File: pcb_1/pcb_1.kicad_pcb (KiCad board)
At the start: 2 copper layers, 80 parts, among them J1 Screw_Terminal_01x02, J2 Screw_Terminal_01x03, J3 Conn_01x02_Male, J4 Screw_Terminal_01x02, J5 Isolated_ISP, J6 AVR-ISP-6, J7 THERM0, J8 THERM1, K1 DIPxx-1Axx-11x, Q1 BD139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

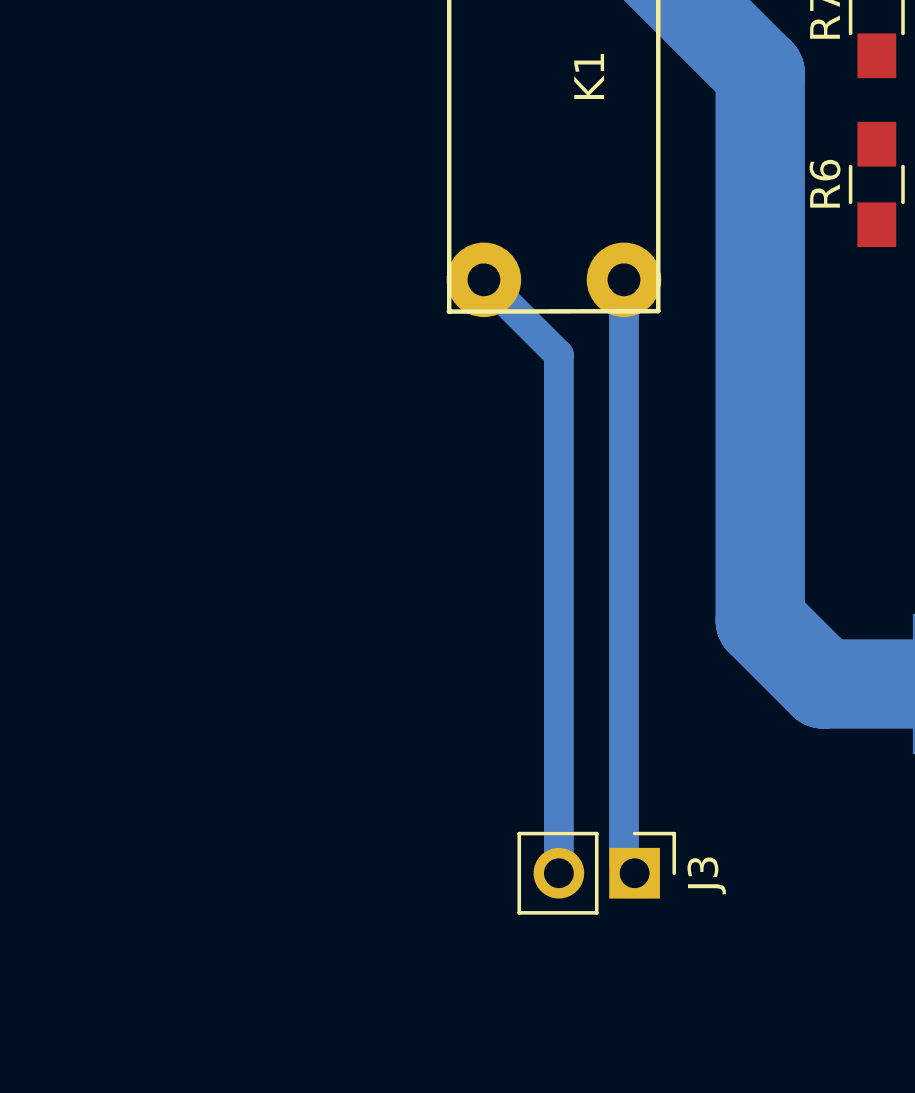
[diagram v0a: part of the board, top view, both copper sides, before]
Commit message: pcb: Releen ohjauspiiri lisätty
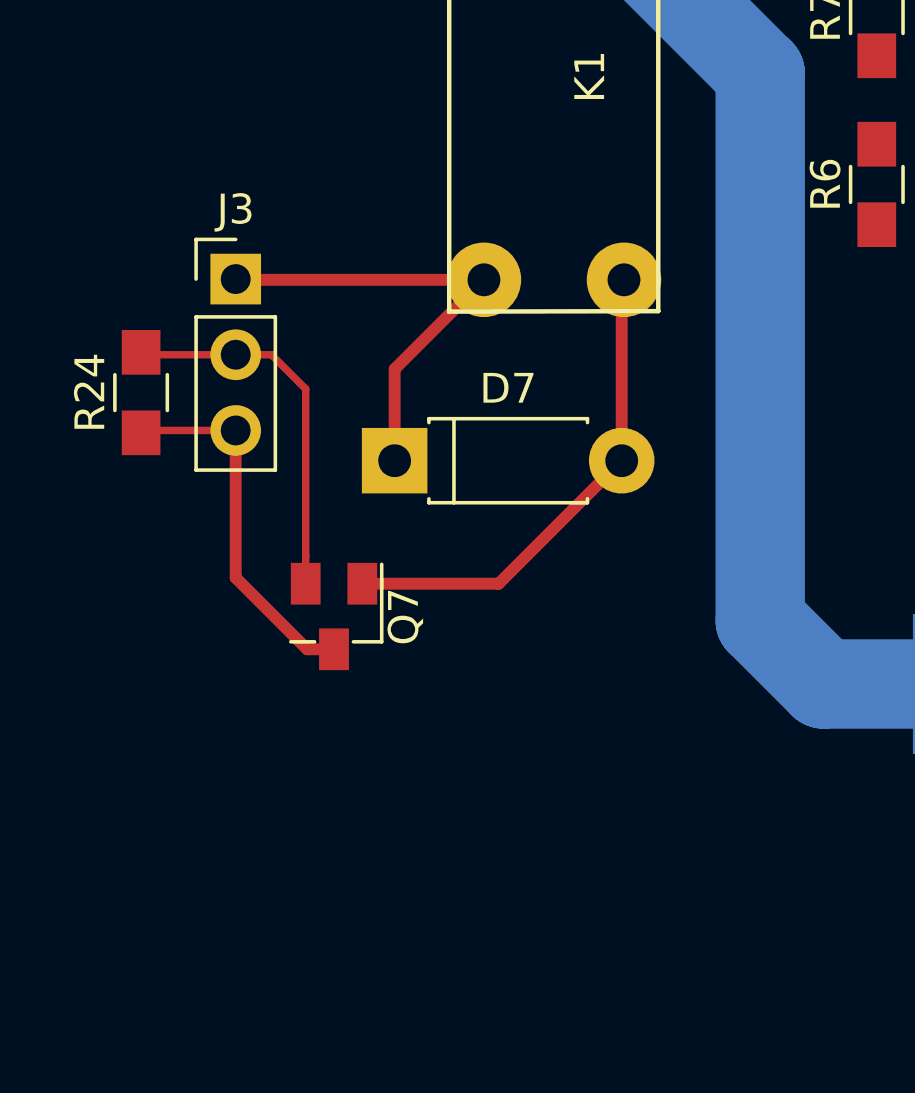
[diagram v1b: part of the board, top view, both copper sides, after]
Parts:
- added D7: D, Diodes_THT:D_DO-41_SOD81_P7.62mm_Horizontal, F.Cu at (25.8, 89.5)
- added Q7: Q_NMOS_DGS, TO_SOT_Packages_SMD:SuperSOT-3, F.Cu at (23.7, 94.8)
- added R24: 100k, Resistors_SMD:R_0805_HandSoldering, F.Cu at (17.3, 87.2)
- J3: value Conn_01x02_Male -> Conn_Relay; footprint Pin_Headers:Pin_Header_Straight_1x02_Pitch2.54mm -> Pin_Headers:Pin_Header_Straight_1x03_Pitch2.54mm
- moved J3 24.0 mm to (20.4, 83.4), turned to 0 degrees
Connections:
- J3 pad 1: Net-(J3-Pad1) -> Net-(D7-Pad1)
- J5 pad 2: Net-(C12-Pad1) -> (no net)
- J5 pad 4: Net-(J5-Pad4) -> (no net)
- J5 pad 6: Net-(C12-Pad2) -> (no net)
- J5 pad 8: Net-(J5-Pad8) -> (no net)
- K1 pad 2: Net-(J3-Pad2) -> Net-(D7-Pad1)
- K1 pad 6: Net-(J3-Pad1) -> Net-(D7-Pad2)
- Q2 pad 2: Net-(J5-Pad4) -> (no net)
- U3 pad 4: Net-(U3-Pad4) -> (no net)
- U8 pad 1: Net-(U8-Pad1) -> (no net)
- U8 pad 4: Net-(U8-Pad4) -> (no net)
- U9 pad 1: Net-(U9-Pad1) -> (no net)
- U9 pad 10: Net-(U9-Pad10) -> (no net)
- U9 pad 11: Net-(U9-Pad11) -> (no net)
- U9 pad 12: Net-(U9-Pad12) -> (no net)
- U9 pad 13: Net-(U9-Pad13) -> (no net)
- U9 pad 2: Net-(U9-Pad2) -> (no net)
- U9 pad 23: Net-(U9-Pad23) -> (no net)
- U9 pad 30: Net-(U9-Pad30) -> (no net)
- U9 pad 31: Net-(U9-Pad31) -> (no net)
- U9 pad 32: Net-(U9-Pad32) -> (no net)
- U9 pad 7: Net-(U9-Pad7) -> (no net)
- U9 pad 8: Net-(U9-Pad8) -> (no net)
- U9 pad 9: Net-(U9-Pad9) -> (no net)
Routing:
- net Net-(J3-Pad1): track 20.1 -> 0.00 mm
- net Net-(D7-Pad2): track 0.00 -> 16.5 mm
- net Net-(D7-Pad1): track 0.00 -> 15.7 mm
- net Net-(J3-Pad3): track 0.00 -> 12.4 mm
- net Net-(J3-Pad2): track 21.0 -> 12.6 mm

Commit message: pcb: Kaikki vedot tehty
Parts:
- C15: value C -> 0.1u
- C2: footprint Capacitors_THT:CP_Radial_D8.0mm_P5.00mm -> Capacitors_SMD:C_1206_HandSoldering
- C6, C8: value C -> 10u; footprint Capacitors_SMD:C_0805_HandSoldering -> Capacitors_SMD:C_1206_HandSoldering
- Rs1: footprint Resistors_SMD:R_2816 -> Resistors_SMD:R_2512_HandSoldering
- moved R24 171.6 mm to (188.0, 104.6), turned to 180 degrees
- moved Q7 167.1 mm to (190.9, 94.0)
- moved J3 164.6 mm to (184.3, 99.8), turned to 90 degrees
- moved D7 158.5 mm to (184.3, 88.9)
- moved J4 157.6 mm to (189.0, 50.4)
- moved K1 155.5 mm to (189.0, 83.0)
- moved R7 138.0 mm to (179.6, 64.8)
- moved R6 137.9 mm to (179.6, 70.9)
- moved J5 137.0 mm to (41.2, 54.3)
- moved J1 136.3 mm to (40.9, 104.6)
- moved D6 133.7 mm to (177.0, 58.2)
- moved Rs1 122.9 mm to (170.4, 96.5), turned to 0 degrees
- moved U3 118.4 mm to (170.3, 88.6), turned to 180 degrees
- moved R10 110.6 mm to (54.9, 60.5), turned to 0 degrees
- moved R12 110.0 mm to (54.9, 67.1), turned to 0 degrees
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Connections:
- C10 pad 2: Iset -> Vset
- C11 pad 2: Vset -> Iset
- C12 pad 1: Net-(C12-Pad1) -> +5V
- C12 pad 2: Net-(C12-Pad2) -> GNDA
- C13 pad 1: Net-(C12-Pad1) -> +5V
- C13 pad 2: Net-(C12-Pad2) -> GNDA
- C14 pad 2: GNDD -> GNDA
- C15 pad 1: GNDD -> GNDA
- C16 pad 2: GNDD -> GNDA
- C17 pad 1: GNDD -> Net-(C17-Pad1)
- C17 pad 2: +5V -> Net-(C17-Pad2)
- J5 pad 2: (no net) -> Net-(C17-Pad2)
- J5 pad 4: (no net) -> Net-(J5-Pad4)
- J5 pad 6: (no net) -> Net-(C17-Pad1)
- J6 pad 6: GNDD -> GNDA
- J7 pad 2: GNDD -> GNDA
- J8 pad 2: GNDD -> GNDA
- Q2 pad 2: (no net) -> Net-(J5-Pad4)
- Q2 pad 3: Net-(C12-Pad2) -> Net-(C17-Pad1)
- Q3 pad 2: Net-(J5-Pad3) -> Net-(J5-Pad5)
- Q3 pad 3: Net-(C12-Pad2) -> Net-(C17-Pad1)
- Q4 pad 2: Net-(J5-Pad5) -> Net-(J5-Pad3)
- Q4 pad 3: Net-(C12-Pad2) -> Net-(C17-Pad1)
- Q5 pad 3: Net-(C12-Pad2) -> Net-(C17-Pad1)
- Q6 pad 3: GNDD -> GNDA
- R10 pad 1: Net-(C12-Pad1) -> Net-(C17-Pad2)
- R11 pad 1: Net-(C12-Pad1) -> Net-(C17-Pad2)
- R12 pad 1: Net-(C12-Pad1) -> Net-(C17-Pad2)
- R13 pad 1: Net-(C12-Pad1) -> Net-(C17-Pad2)
- R19 pad 2: Net-(J7-Pad1) -> Net-(J8-Pad1)
- R20 pad 2: Net-(J8-Pad1) -> Net-(J7-Pad1)
- R8 pad 1: Iset -> Vset
- R9 pad 1: Vset -> Iset
- U1 pad 1: Net-(C1-Pad2) -> Net-(C4-Pad1)
- U1 pad 2: Vmon -> Imon
- U1 pad 3: Vset -> Iset
- U1 pad 5: Iset -> Vset
- U1 pad 6: Imon -> Vmon
- U1 pad 7: Net-(C4-Pad1) -> Net-(C1-Pad2)
- U6 pad 2: Net-(C12-Pad2) -> Net-(C17-Pad1)
- U6 pad 3: Net-(C12-Pad2) -> Net-(C17-Pad1)
- U6 pad 5: Net-(C12-Pad2) -> GNDA
- U6 pad 7: SLAVE_SCK -> SLAVE_RESET
- U6 pad 8: Net-(C12-Pad1) -> +5V
- U7 pad 1: Net-(Q5-Pad1) -> Net-(Q4-Pad1)
- U7 pad 2: Net-(C12-Pad2) -> Net-(C17-Pad1)
- U7 pad 3: Net-(C12-Pad2) -> Net-(C17-Pad1)
- U7 pad 4: Net-(Q4-Pad1) -> Net-(Q5-Pad1)
- U7 pad 5: Net-(C12-Pad2) -> GNDA
- U7 pad 6: SLAVE_RESET -> SLAVE_CS
- U7 pad 7: SLAVE_CS -> SLAVE_SCK
- U7 pad 8: Net-(C12-Pad1) -> +5V
- U8 pad 3: GNDD -> GNDA
- U8 pad 5: GNDD -> Net-(C17-Pad1)
- U8 pad 7: +5V -> Net-(C17-Pad2)
- U8 pad 8: +5V -> Net-(C17-Pad2)
- U9 pad 21: GNDD -> GNDA
- U9 pad 26: UNREG_MON -> Net-(J8-Pad1)
- U9 pad 28: Net-(J8-Pad1) -> UNREG_MON
- U9 pad 5: GNDD -> GNDA
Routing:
- net +5V: track 0.00 -> 299.1 mm
- net ADC_SCL: track 0.00 -> 139.2 mm, vias 0 -> 2
- net ADC_SDA: track 0.00 -> 101.4 mm
- net Net-(CP1-Pad1): track 94.0 -> 164.6 mm
- net Net-(C17-Pad2): track 0.00 -> 66.3 mm, vias 0 -> 4
- net SLAVE_CS: track 0.00 -> 63.3 mm, vias 0 -> 2
- net Net-(J8-Pad1): track 0.00 -> 53.6 mm
- net Net-(J7-Pad1): track 0.00 -> 53.4 mm
- net Vmon: track 0.00 -> 48.6 mm, vias 0 -> 2
- net DAC_CS: track 0.00 -> 40.1 mm, vias 0 -> 2
- net Imon: track 0.00 -> 39.7 mm
- net UNREG_MON: track 0.00 -> 38.0 mm, vias 0 -> 2
- net SLAVE_MOSI: track 0.00 -> 37.6 mm
- net DAC_LDAC: track 0.00 -> 36.1 mm, vias 0 -> 2
- net Net-(C2-Pad1): track 0.00 -> 33.7 mm
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- added copper zone on B.Cu, net GNDA
- added copper zone on F.Cu, net GNDA
- added copper zone on B.Cu, net Net-(C17-Pad1)
- added copper zone on F.Cu, net Net-(C17-Pad1)

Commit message: Toinen konkka lisätty
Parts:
- added C18: CP, Capacitors_THT:CP_Radial_D30.0mm_P10.00mm_SnapIn, F.Cu at (87.4, 99.5)
- moved TP1 52.7 mm to (144.0, 95.0)
- moved D5 27.9 mm to (89.2, 74.7), turned to 0 degrees
- moved F1 21.1 mm to (61.2, 89.4)
- moved D1 14.9 mm to (67.0, 96.7), turned to 270 degrees
- moved J1 2.25 mm to (42.7, 106.0)
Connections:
- J5 pad 2: Net-(C17-Pad2) -> Net-(J5-Pad2)
- J5 pad 6: Net-(C17-Pad1) -> Net-(J5-Pad6)
- J5 pad 8: (no net) -> Net-(J5-Pad8)
- Q2 pad 2: Net-(J5-Pad4) -> Net-(Q2-Pad2)
- U3 pad 4: (no net) -> Net-(U3-Pad4)
- U8 pad 1: (no net) -> Net-(U8-Pad1)
- U8 pad 4: (no net) -> Net-(U8-Pad4)
- U9 pad 1: (no net) -> Net-(U9-Pad1)
- U9 pad 10: (no net) -> Net-(U9-Pad10)
- U9 pad 11: (no net) -> Net-(U9-Pad11)
- U9 pad 12: (no net) -> Net-(U9-Pad12)
- U9 pad 13: (no net) -> Net-(U9-Pad13)
- U9 pad 2: (no net) -> Net-(U9-Pad2)
- U9 pad 23: (no net) -> Net-(U9-Pad23)
- U9 pad 30: (no net) -> Net-(U9-Pad30)
- U9 pad 31: (no net) -> Net-(U9-Pad31)
- U9 pad 32: (no net) -> Net-(U9-Pad32)
- U9 pad 7: (no net) -> Net-(U9-Pad7)
- U9 pad 8: (no net) -> Net-(U9-Pad8)
- U9 pad 9: (no net) -> Net-(U9-Pad9)
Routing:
- net Net-(C18-Pad1): track 164.6 -> 211.5 mm
- net Net-(D1-Pad3): track 42.0 -> 27.1 mm
- net Net-(C5-Pad1): track 27.9 -> 14.3 mm
- net Net-(F1-Pad2): track 23.0 -> 13.0 mm
- net Net-(D1-Pad2): track 14.3 -> 10.2 mm

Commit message: pcb: Rescue kirjasto poistettu
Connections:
- J5 pad 2: Net-(J5-Pad2) -> Net-(C17-Pad2)
- J5 pad 6: Net-(J5-Pad6) -> Net-(C17-Pad1)
- J5 pad 8: Net-(J5-Pad8) -> (no net)
- Q2 pad 2: Net-(Q2-Pad2) -> Net-(J5-Pad4)
- U3 pad 4: Net-(U3-Pad4) -> (no net)
- U8 pad 1: Net-(U8-Pad1) -> (no net)
- U8 pad 4: Net-(U8-Pad4) -> (no net)
- U9 pad 1: Net-(U9-Pad1) -> (no net)
- U9 pad 10: Net-(U9-Pad10) -> (no net)
- U9 pad 11: Net-(U9-Pad11) -> (no net)
- U9 pad 12: Net-(U9-Pad12) -> (no net)
- U9 pad 13: Net-(U9-Pad13) -> (no net)
- U9 pad 2: Net-(U9-Pad2) -> (no net)
- U9 pad 23: Net-(U9-Pad23) -> (no net)
- U9 pad 30: Net-(U9-Pad30) -> (no net)
- U9 pad 31: Net-(U9-Pad31) -> (no net)
- U9 pad 32: Net-(U9-Pad32) -> (no net)
- U9 pad 7: Net-(U9-Pad7) -> (no net)
- U9 pad 8: Net-(U9-Pad8) -> (no net)
- U9 pad 9: Net-(U9-Pad9) -> (no net)

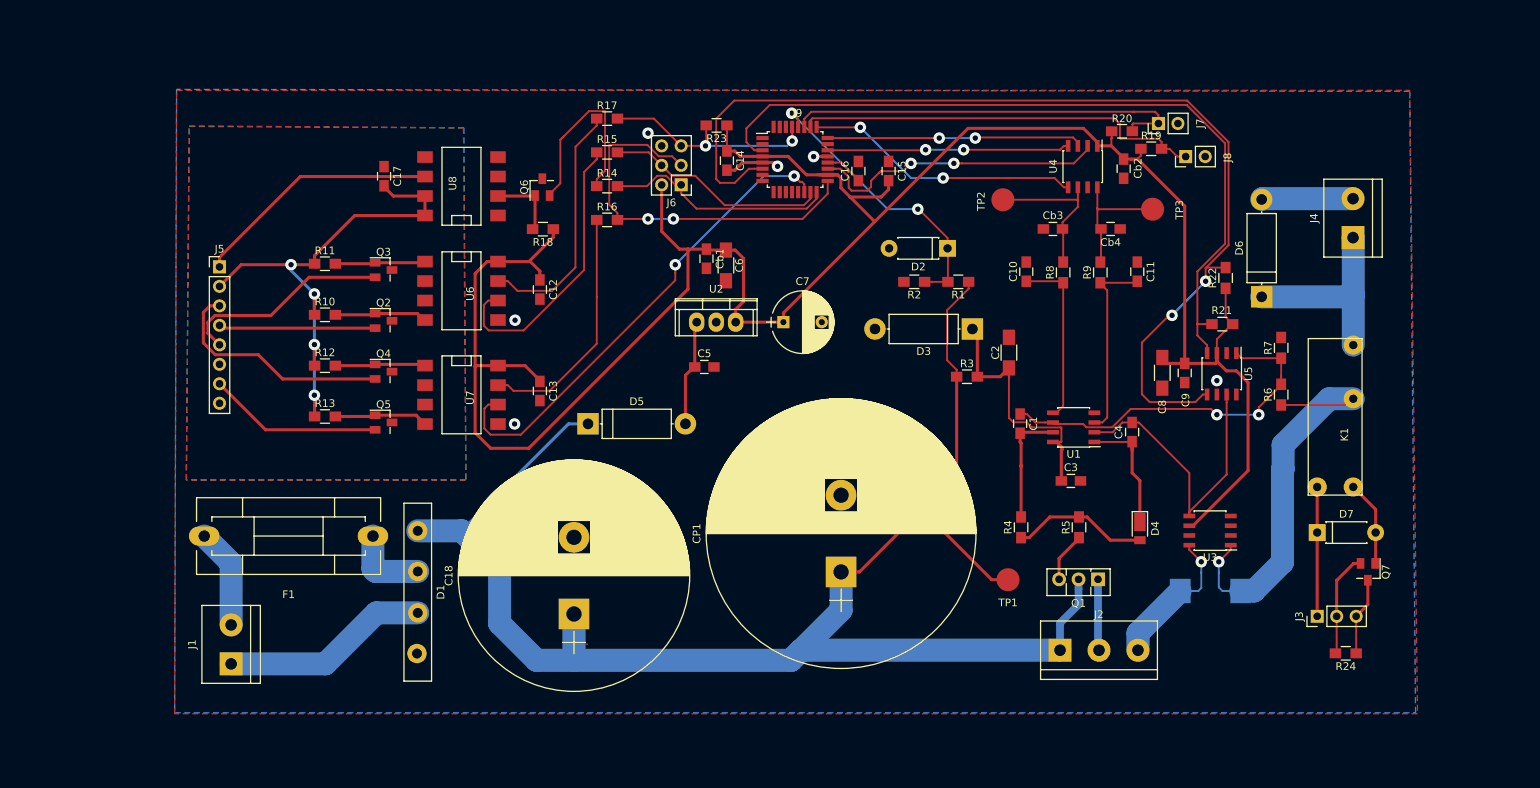
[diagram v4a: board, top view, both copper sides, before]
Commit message: pcb: Suodatuskonkat ja kiinnitysreiät lisätty
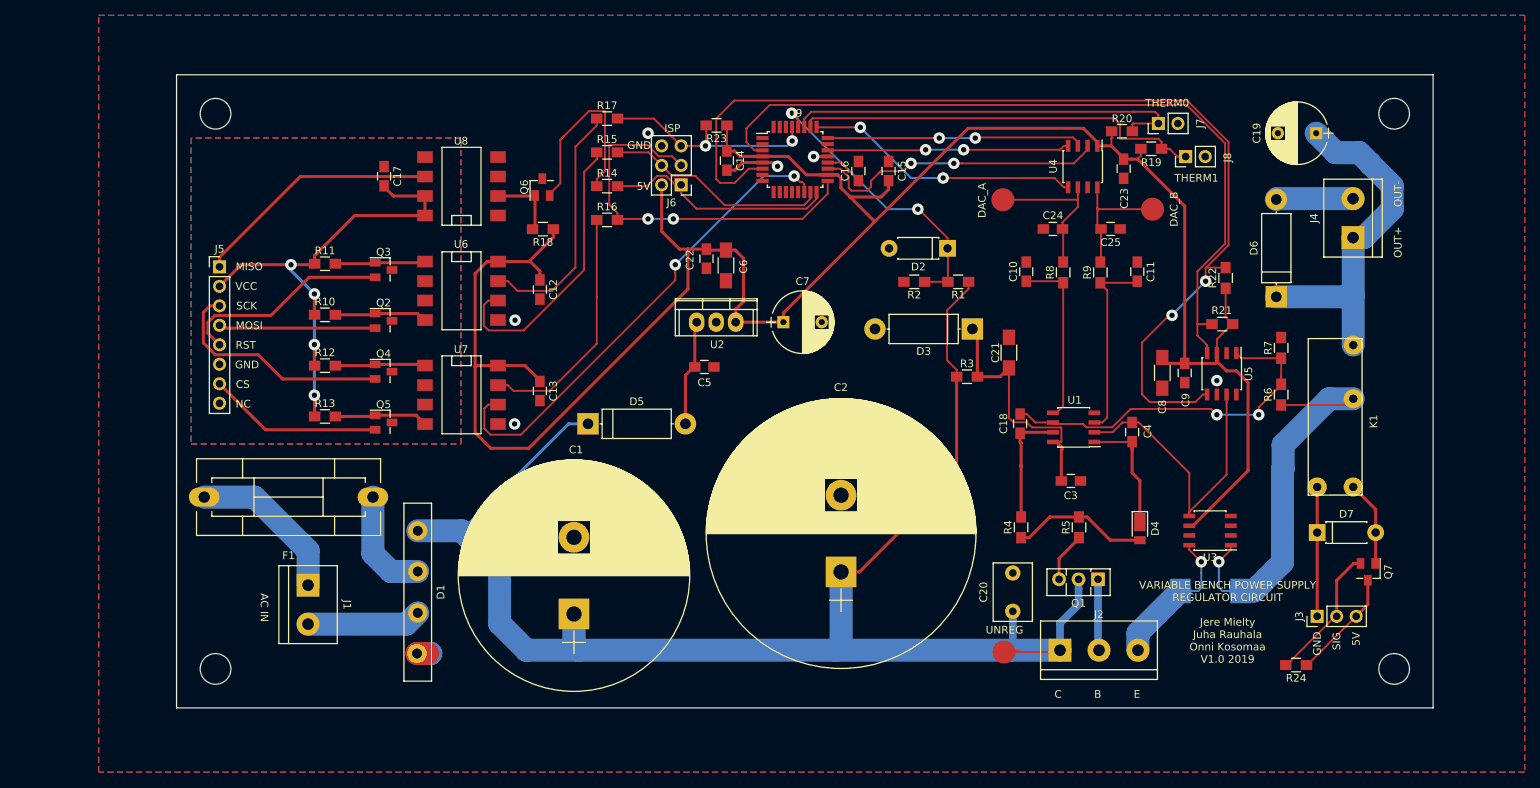
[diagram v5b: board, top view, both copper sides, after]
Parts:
- added C19: CP, Capacitors_THT:CP_Radial_D8.0mm_P5.00mm, F.Cu at (184.2, 36.8)
- added C20: C, Capacitors_THT:C_Disc_D7.5mm_W5.0mm_P5.00mm, F.Cu at (144.6, 99.2)
- added REF**: MountingHole_4mm, Mounting_Holes:MountingHole_4mm, F.Cu at (194.3, 34.3)
- added REF**: MountingHole_4mm, Mounting_Holes:MountingHole_4mm, F.Cu at (194.3, 106.7)
- added REF**: MountingHole_4mm, Mounting_Holes:MountingHole_4mm, F.Cu at (40.6, 106.7)
- added REF**: MountingHole_4mm, Mounting_Holes:MountingHole_4mm, F.Cu at (40.6, 34.3)
- C1: renamed from C18; value CP -> 4700u
- C2: renamed from CP1; value 15000uF 50V -> 15000u
- moved J1 14.4 mm to (52.7, 95.8), turned to 270 degrees
- moved TP1 9.44 mm to (143.4, 104.5), turned to 0 degrees
- moved R24 6.65 mm to (181.5, 106.2)
- moved F1 5.08 mm to (61.2, 84.3)
- moved D6 1.91 mm to (178.9, 58.2)
- renumbered C1 to C18, C2 to C21, Cb1 to C22, Cb2 to C23, Cb3 to C24, Cb4 to C25
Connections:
- J1 pad 1: Net-(D1-Pad3) -> Net-(F1-Pad2)
- J1 pad 2: Net-(F1-Pad2) -> Net-(D1-Pad3)
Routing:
- net Net-(C19-Pad1): track 26.1 -> 46.6 mm
- net Net-(D1-Pad3): track 27.1 -> 14.9 mm
- net Net-(F1-Pad2): track 13.0 -> 20.9 mm
- net Net-(C1-Pad1): track 211.5 -> 205.4 mm
- net Net-(J3-Pad2): track 13.6 -> 18.2 mm
- net Net-(J3-Pad3): track 10.2 -> 14.4 mm
- net Net-(D1-Pad2): track 10.2 -> 14.2 mm
- net GNDA: track 21.3 -> 22.6 mm
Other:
- board outline added: 163.8 x 82.6 mm
- board text added: "5V"
- board text added: "AC IN"
- board text added: "B"
- board text added: "C"
- board text added: "CS"
- board text added: "DAC_A"
- board text added: "DAC_B"
- board text added: "E"
- board text added: "GND"
- board text added: "ISP"
- board text added: "MISO"
- board text added: "MOSI"
- board text added: "NC"
- board text added: "OUT+"
- board text added: "OUT-"
- board text added: "RST"
- board text added: "SCK"
- board text added: "SIG"
- board text added: "THERM0"
- board text added: "THERM1"
- board text added: "UNREG"
- board text added: "VARIABLE BENCH POWER SUPPLY REGULATOR CIRCUIT Jere Mielty Juha Rauhala Onni Kosomaa V1.0 2019"
- board text added: "VCC"
